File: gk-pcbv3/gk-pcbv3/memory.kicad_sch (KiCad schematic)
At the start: 25 parts, among them J4 Micro_SD_Card_Det2, U17 S80KS5122GABHI020, U5 S26KS128SDPBHI020, U6 S80KS5122GABHI020, U8 TPS2041BDBV

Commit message: hardware changes
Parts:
- U17, U6: footprint STM32H7S7:PG-BGA-24-801 -> STM32H7S7:BGA24_Hyperbus
- U5: footprint STM32H7S7:BGA24_S26KS512SDPBHI020_CYP_INF -> STM32H7S7:BGA24_Hyperbus
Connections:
- net XSPI1_CK renamed XSPI1_CK_P
- net XSPI1_CK# renamed XSPI1_CK_N
- net XSPI2_CK renamed XSPI2_CK_P
- net XSPI2_CK# renamed XSPI2_CK_N
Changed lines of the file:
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@@
 		)
 	)
-	(global_label "XSPI1_CK"
+	(global_label "XSPI1_CK_P"
 		(shape input)
 		(at 53.34 116.84 180)
@@
 		)
 	)
-	(global_label "XSPI1_CK#"
+	(global_label "XSPI1_CK_N"
 		(shape input)
 		(at 53.34 166.37 180)
@@
 		)
 	)
-	(global_label "XSPI2_CK#"
+	(global_label "XSPI2_CK_N"
 		(shape input)
 		(at 31.75 40.64 180)
@@
 		)
 	)
-	(global_label "XSPI1_CK#"
+	(global_label "XSPI1_CK_N"
 		(shape input)
 		(at 53.34 119.38 180)
@@
 		)
 	)
-	(global_label "XSPI1_CK"
+	(global_label "XSPI1_CK_P"
 		(shape input)
 		(at 53.34 163.83 180)
@@
 		)
 	)
-	(global_label "XSPI2_CK"
+	(global_label "XSPI2_CK_P"
 		(shape input)
 		(at 31.75 38.1 180)
@@
 			)
 		)
-		(property "Footprint" "STM32H7S7:PG-BGA-24-801"
+		(property "Footprint" "STM32H7S7:BGA24_Hyperbus"
 			(at 53.34 163.83 0)
 			(effects
@@
 			)
 		)
-		(property "Footprint" "STM32H7S7:BGA24_S26KS512SDPBHI020_CYP_INF"
+		(property "Footprint" "STM32H7S7:BGA24_Hyperbus"
 			(at 102.87 36.83 0)
 			(effects
@@
 			)
 		)
-		(property "Footprint" "STM32H7S7:PG-BGA-24-801"
+		(property "Footprint" "STM32H7S7:BGA24_Hyperbus"
 			(at 166.37 120.65 0)
 			(effects
@@
 			)
 		)
-		(property "Footprint" "STM32H7S7:BGA24_S26KS512SDPBHI020_CYP_INF"
+		(property "Footprint" "STM32H7S7:BGA24_Hyperbus"
 			(at 31.75 38.1 0)
 			(effects
@@
 			)
 		)
-		(property "Footprint" "STM32H7S7:PG-BGA-24-801"
+		(property "Footprint" "STM32H7S7:BGA24_Hyperbus"
 			(at 156.21 120.65 0)
 			(effects
@@
 			)
 		)
-		(property "Footprint" "STM32H7S7:PG-BGA-24-801"
+		(property "Footprint" "STM32H7S7:BGA24_Hyperbus"
 			(at 53.34 116.84 0)
 			(effects

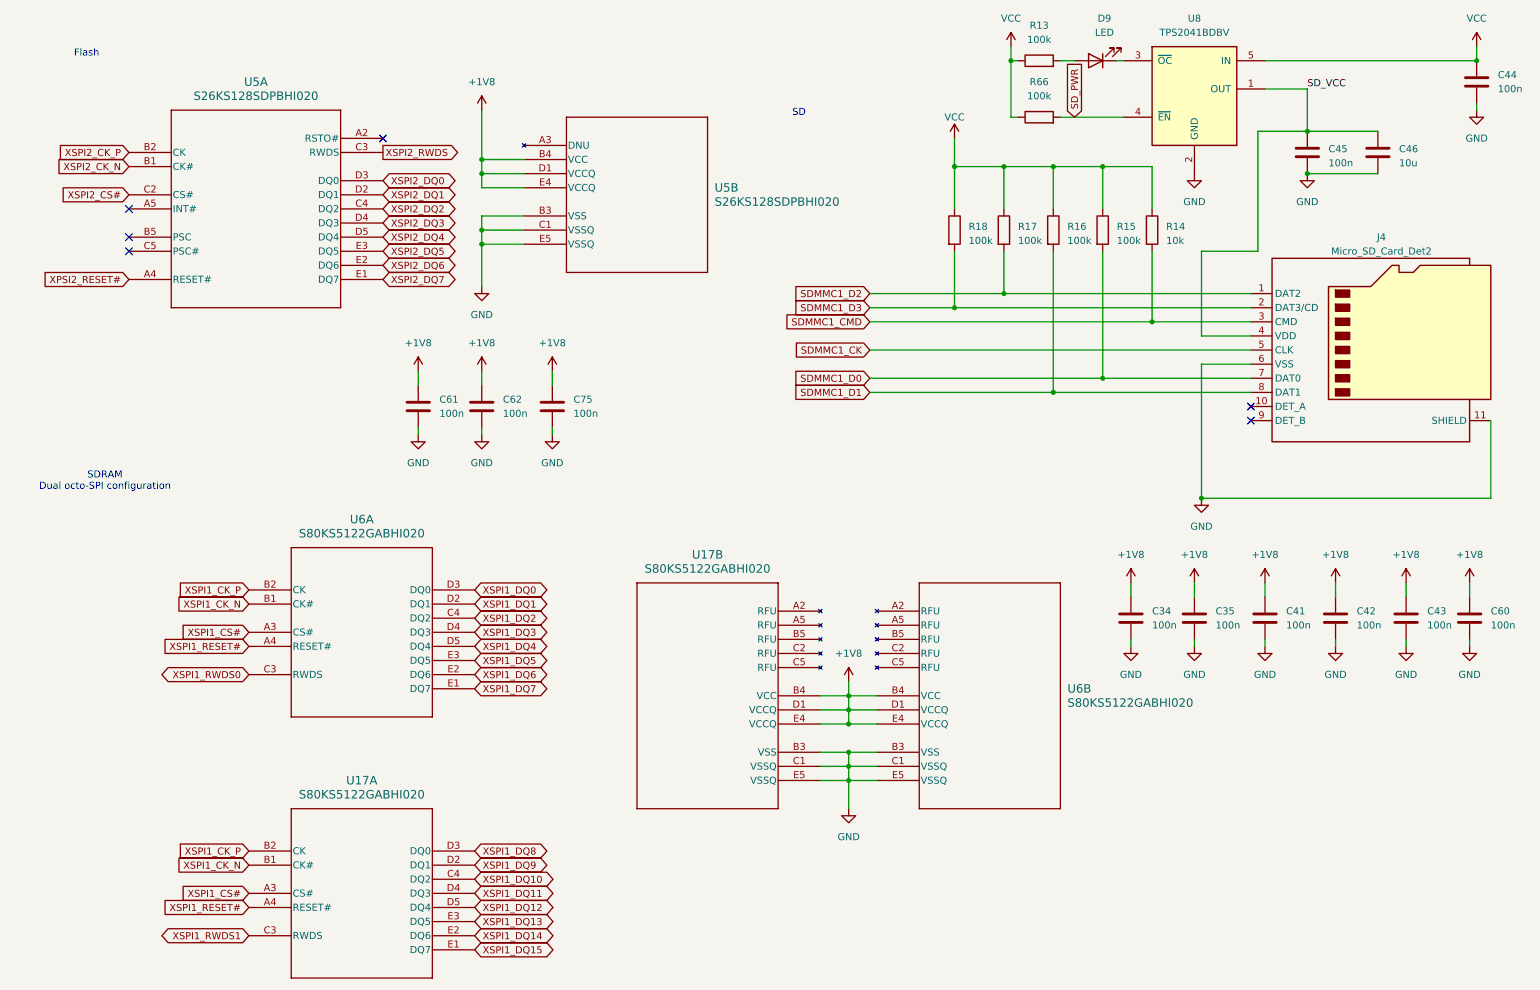
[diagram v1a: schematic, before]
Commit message: redesign for better signal integrity
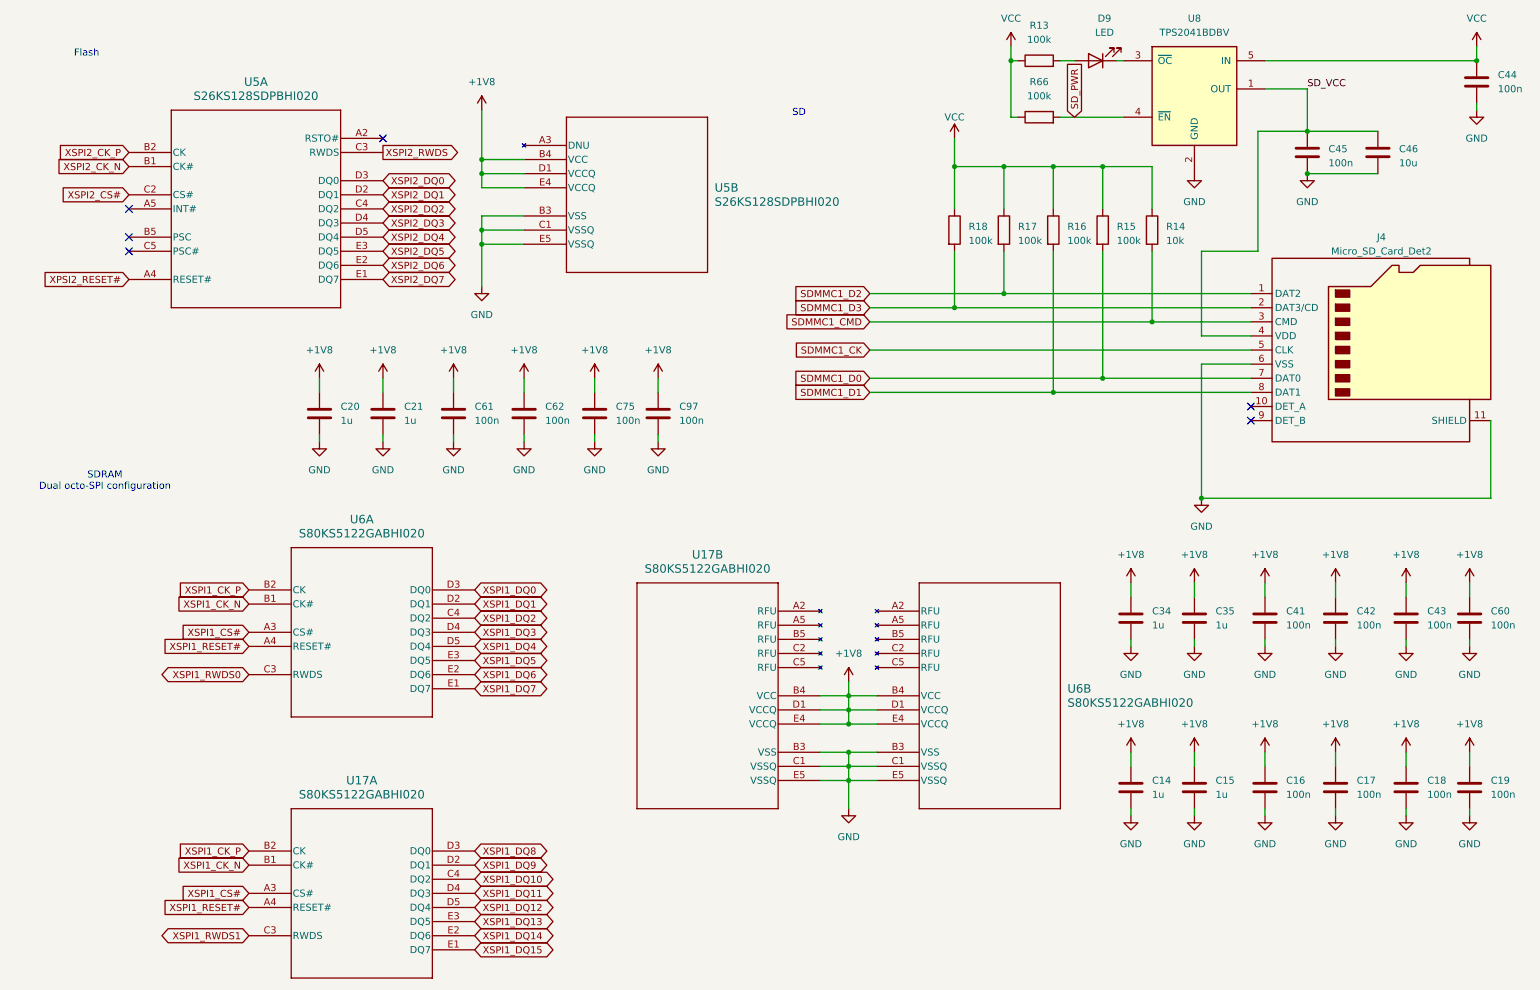
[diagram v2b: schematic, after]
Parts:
- added C14, C15, C20, C21: 1u, Capacitor_SMD:C_0402_1005Metric, symbol Device:C
- added C16, C17, C18, C19, C97: 100n, Capacitor_SMD:C_0402_1005Metric, symbol Device:C
- C34, C35: value 100n -> 1u; footprint Capacitor_SMD:C_0603_1608Metric -> Capacitor_SMD:C_0402_1005Metric
- C41, C42, C43, C60, C61, C62, C75: footprint Capacitor_SMD:C_0603_1608Metric -> Capacitor_SMD:C_0402_1005Metric
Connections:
- net +1V8: now also C14.1, C15.1, C16.1, C17.1, C18.1, C19.1, C20.1, C21.1, C97.1
- net GND: now also C14.2, C15.2, C16.2, C17.2, C18.2, C19.2, C20.2, C21.2, C97.2
